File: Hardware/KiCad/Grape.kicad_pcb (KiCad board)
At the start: 2 copper layers, 68.6 x 53.3 mm, 105 parts, among them J1 USB_MICROB, J19 POWER_JACKPTH, J3 ARDUINO_R3, P1 CONN_01X03, P10 CONN_01X03, P11 CONN_01X03, P12 CONN_01X03, P13 CONN_01X03, P14 CONN_01X03, P15 CONN_01X03, P16 CONN_01X03, P17 CONN_01X03, P18 CONN_01X03, P19 CONN_01X03, P2 CONN_01X03, P20 CONN_01X03, P21 CONN_01X03, P22 CONN_01X03, P23 I2C, P3 CONN_01X03, P4 CONN_01X03, P5 CONN_01X03, P6 CONN_01X03, P7 CONN_01X03, P8 CONN_01X03, P9 CONN_01X03, Q1 2N7002PW, Q4 FDN340P, Q5 FDN340P, SW1 SW_SPDT, U1 FT231XS, U2 LM358, U3 AMS1117-3.3, U4 ATMEGA328P_TQFP, U8 MP2307SO, Y1 16MHz

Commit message: Valores cambiados
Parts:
- C1, C2, C4, C5, C6: value 0.1uF -> 100nF
- C15: value 100n -> 100nF
- C16: value 10n -> 10nF
- C3: value CP1_SmalluF -> 10nF
- C7: value 100u -> 100uF
- C8: value 3.3n -> 3.3nF
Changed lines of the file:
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@@
       (effects (font (size 1 1) (thickness 0.15)))
     )
-    (fp_text value 0.1uF (at 0 1.75 180) (layer F.Fab)
+    (fp_text value 100nF (at 0 1.75 180) (layer F.Fab)
       (effects (font (size 1 1) (thickness 0.15)))
     )
@@
       (effects (font (size 1 1) (thickness 0.15)))
     )
-    (fp_text value 0.1uF (at 0 1.75 180) (layer F.Fab)
+    (fp_text value 100nF (at 0 1.75 180) (layer F.Fab)
       (effects (font (size 1 1) (thickness 0.15)))
     )
@@
       (effects (font (size 1 1) (thickness 0.15)))
     )
-    (fp_text value CP1_SmalluF (at 0 2.55 180) (layer F.Fab)
+    (fp_text value 10nF (at 0 2.55 180) (layer F.Fab)
       (effects (font (size 1 1) (thickness 0.15)))
     )
@@
       (effects (font (size 1 1) (thickness 0.15)))
     )
-    (fp_text value 0.1uF (at 0 1.75) (layer F.Fab)
+    (fp_text value 100nF (at 0 1.75) (layer F.Fab)
       (effects (font (size 1 1) (thickness 0.15)))
     )
@@
       (effects (font (size 1 1) (thickness 0.15)))
     )
-    (fp_text value 0.1uF (at 0 1.5) (layer F.Fab)
+    (fp_text value 100nF (at 0 1.5) (layer F.Fab)
       (effects (font (size 1 1) (thickness 0.15)))
     )
@@
       (effects (font (size 1 1) (thickness 0.15)))
     )
-    (fp_text value 0.1uF (at 0 1.5) (layer F.Fab)
+    (fp_text value 100nF (at 0 1.5) (layer F.Fab)
       (effects (font (size 1 1) (thickness 0.15)))
     )
@@
       (effects (font (size 1 1) (thickness 0.15)))
     )
-    (fp_text value 100u (at 0 -4.56) (layer F.Fab)
+    (fp_text value 100uF (at 0 -4.56) (layer F.Fab)
       (effects (font (size 1 1) (thickness 0.15)))
     )
@@
       (effects (font (size 1 1) (thickness 0.15)))
     )
-    (fp_text value 3.3n (at 0 1.75) (layer F.Fab)
+    (fp_text value 3.3nF (at 0 1.75) (layer F.Fab)
       (effects (font (size 1 1) (thickness 0.15)))
     )
@@
       (effects (font (size 1 1) (thickness 0.15)))
     )
-    (fp_text value 100n (at 0 1.75) (layer F.Fab)
+    (fp_text value 100nF (at 0 1.75) (layer F.Fab)
       (effects (font (size 1 1) (thickness 0.15)))
     )
@@
       (effects (font (size 1 1) (thickness 0.15)))
     )
-    (fp_text value 10n (at 0 1.75 90) (layer F.Fab)
-      (effects (font (size 1 1) (thickness 0.15)))
-    )
+    (fp_text value 10nF (at 0 1.75 90) (layer F.Fab)
+      (effects (font (size 1 1) (thickness 0.15)))
+    )

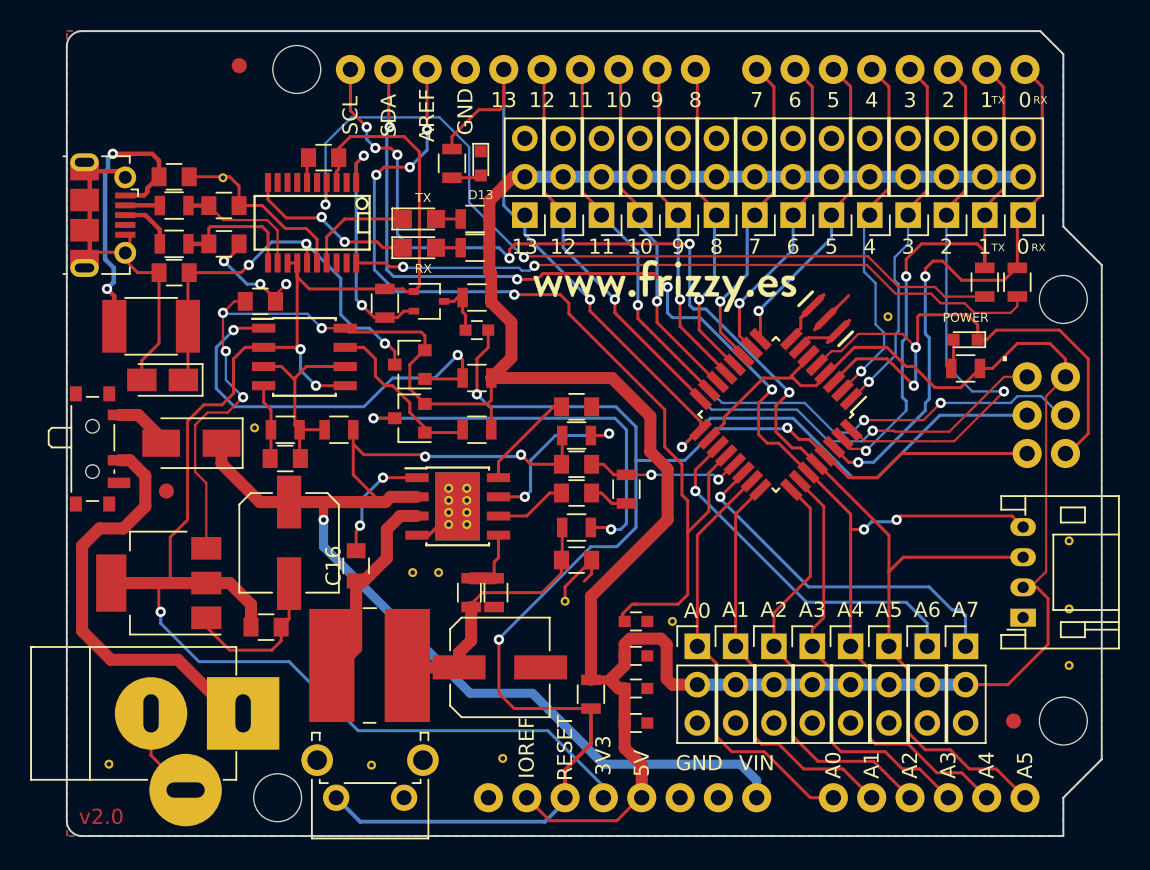
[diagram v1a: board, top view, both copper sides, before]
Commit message: Añadida serigrafia en PWM pins
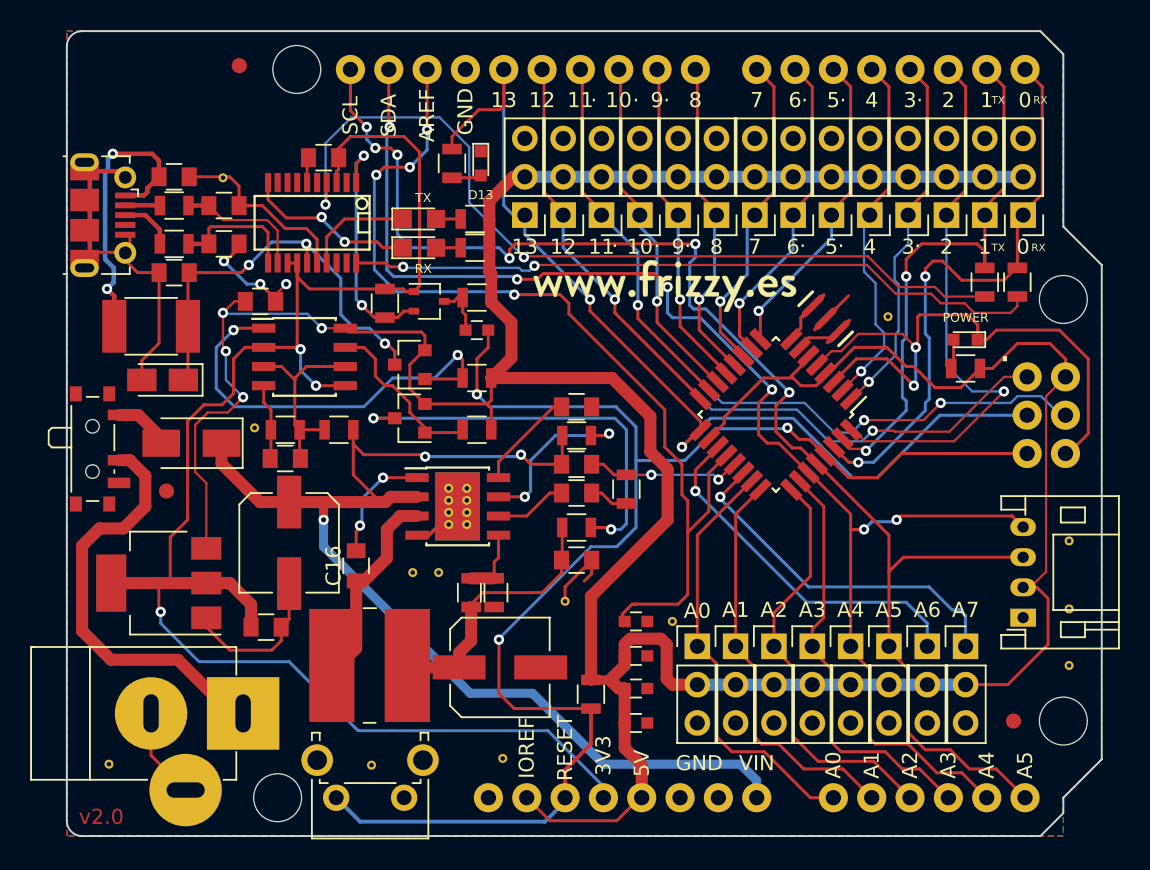
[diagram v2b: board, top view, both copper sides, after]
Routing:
- net AD5/SCL: track 92.5 -> 93.0 mm
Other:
- outline, holes or cut-outs redrawn
